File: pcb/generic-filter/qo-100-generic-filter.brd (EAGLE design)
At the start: 53 x 20 mm, 35 parts

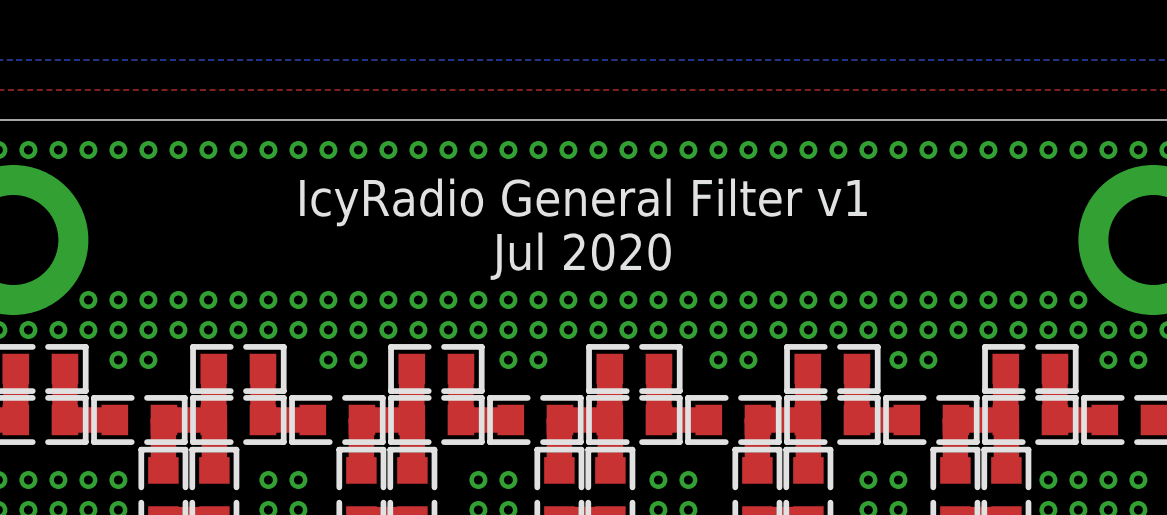
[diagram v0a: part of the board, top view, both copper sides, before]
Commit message: Change upconverter input attenuation Rename general filter to generic filter Generate generic filter panel Change capacitor value on LNB controller Add PA gain response
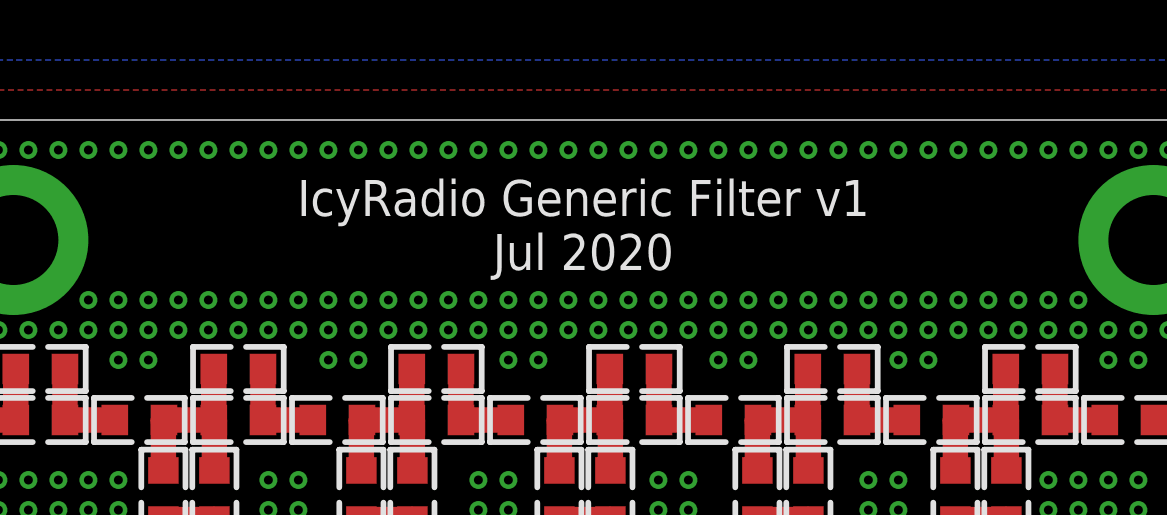
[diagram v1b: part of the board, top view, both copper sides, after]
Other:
- board text added: "IcyRadio Generic Filter v1 Jul 2020"
- board text removed: "IcyRadio General Filter v1 Jul 2020"
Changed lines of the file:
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@@
 <wire x1="0" y1="19" x2="0" y2="1" width="0" layer="20"/>
 <wire x1="0" y1="1" x2="1" y2="0" width="0" layer="20" curve="90"/>
-<text x="26.5" y="16.5" size="1.2" layer="21" font="vector" ratio="10" align="center">IcyRadio General Filter v1
+<text x="26.5" y="16.5" size="1.2" layer="21" font="vector" ratio="10" align="center">IcyRadio Generic Filter v1
 Jul 2020</text>
 </plain>
